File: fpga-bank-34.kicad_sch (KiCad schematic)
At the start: 5 parts

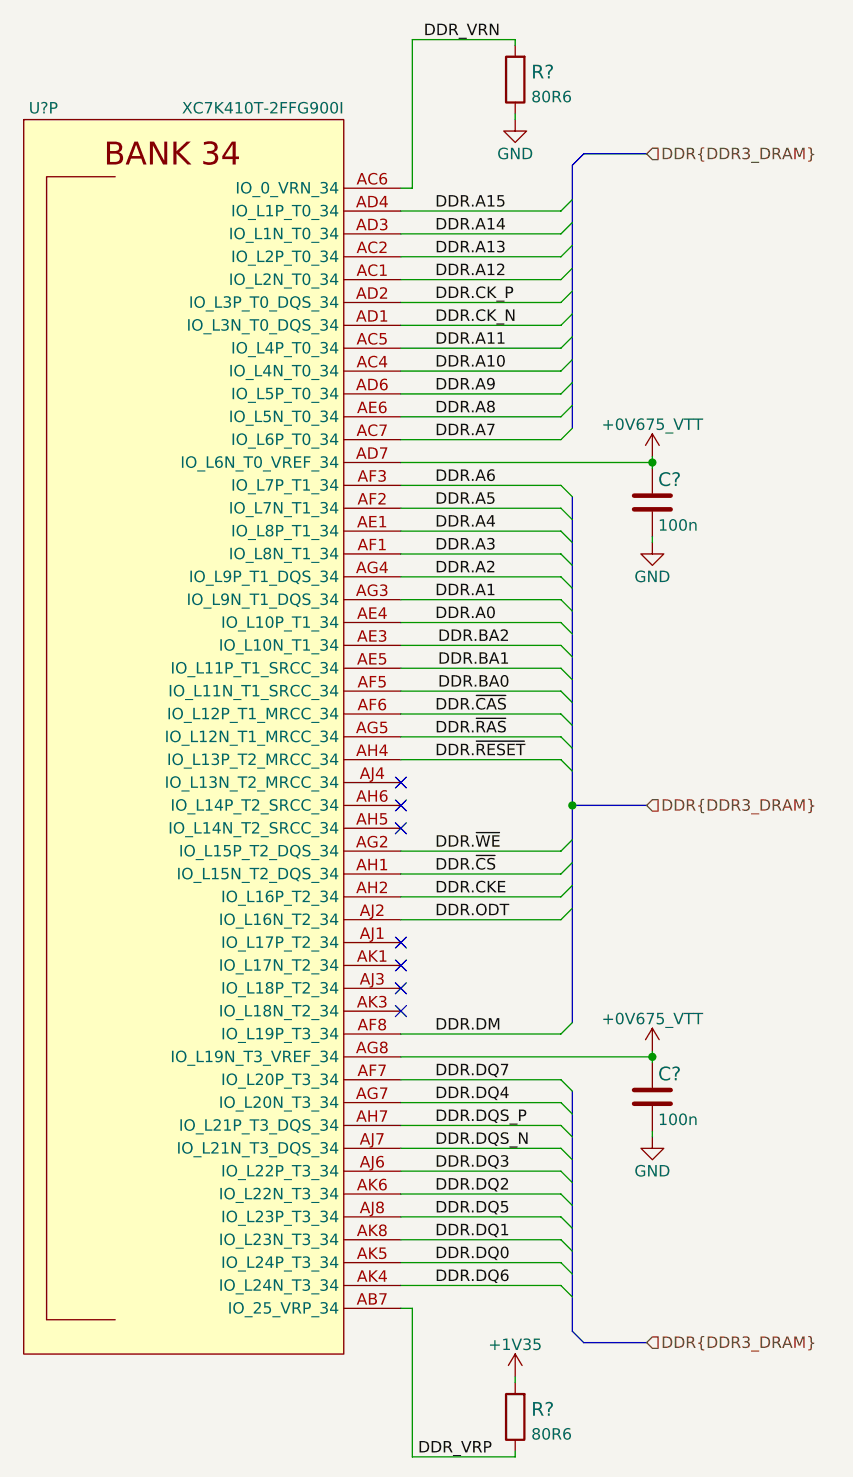
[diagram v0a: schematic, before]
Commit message: Fix FPGA symbol
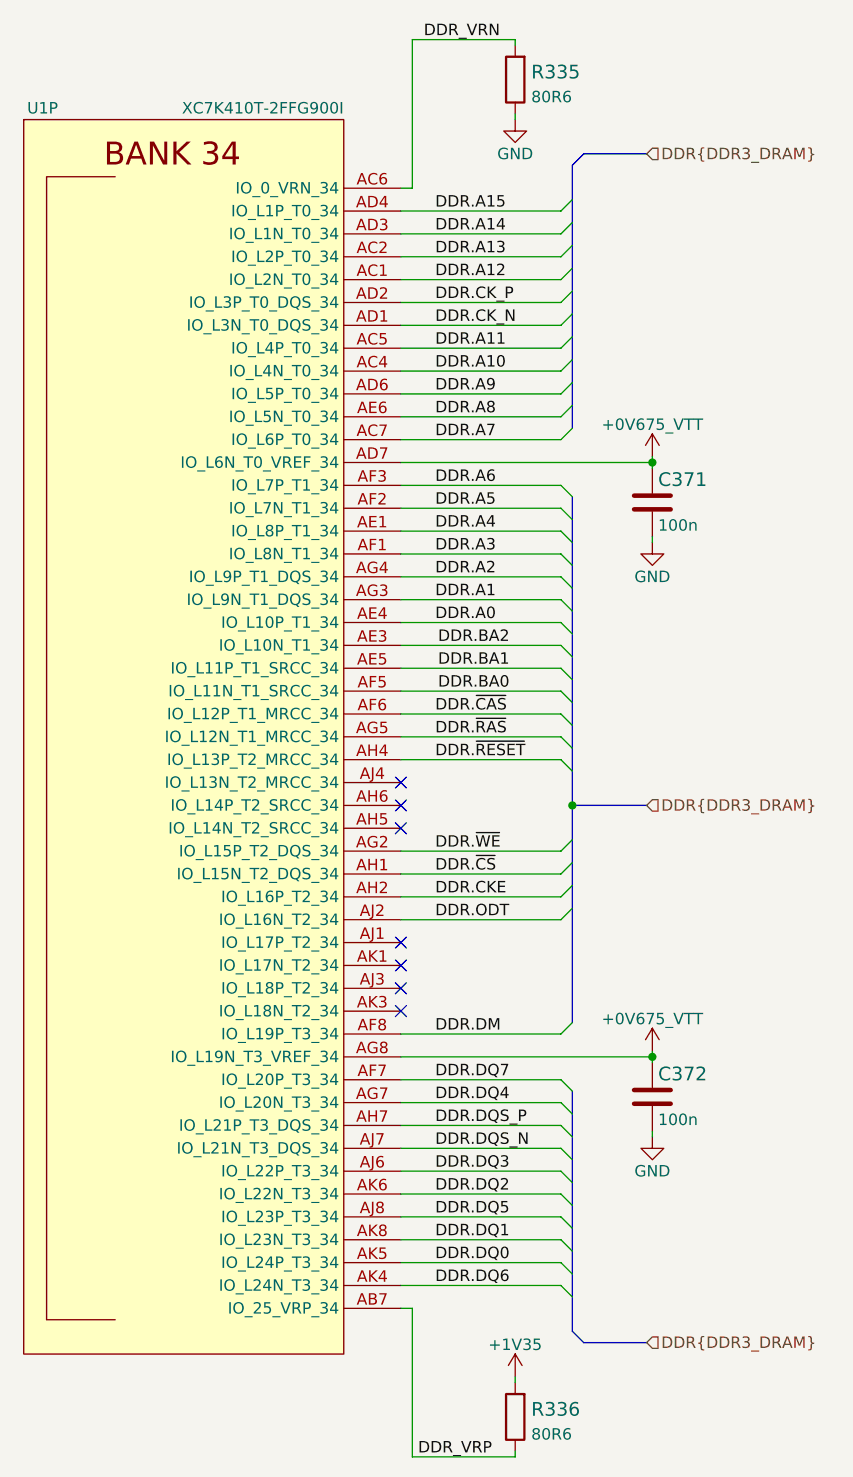
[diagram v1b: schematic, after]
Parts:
- gave numbers to parts that had none: 5
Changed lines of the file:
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@@
   (symbol (lib_id "antmicroResistors0402:R_80R6_0402") (at 156.21 71.755 90) (unit 1)
     (in_bom yes) (on_board yes) (fields_autoplaced)
-    (property "Reference" "R?" (id 0) (at 157.988 70.9204 90)
+    (property "Reference" "R335" (id 0) (at 157.988 70.9204 90)
       (effects (font (size 1.524 1.524)) (justify right))
     )
@@
   (symbol (lib_id "antmicroResistors0402:R_80R6_0402") (at 156.21 220.345 90) (unit 1)
     (in_bom yes) (on_board yes) (fields_autoplaced)
-    (property "Reference" "R?" (id 0) (at 157.988 219.5104 90)
+    (property "Reference" "R336" (id 0) (at 157.988 219.5104 90)
       (effects (font (size 1.524 1.524)) (justify right))
     )
@@
   (symbol (lib_id "power:GND") (at 171.45 189.23 0) (unit 1)
     (in_bom yes) (on_board yes)
-    (property "Reference" "#PWR?" (id 0) (at 171.45 195.58 0)
+    (property "Reference" "#PWR0513" (id 0) (at 171.45 195.58 0)
       (effects (font (size 1.27 1.27)) hide)
     )
@@
   (symbol (lib_id "power:GND") (at 171.45 123.19 0) (unit 1)
     (in_bom yes) (on_board yes)
-    (property "Reference" "#PWR?" (id 0) (at 171.45 129.54 0)
+    (property "Reference" "#PWR0512" (id 0) (at 171.45 129.54 0)
       (effects (font (size 1.27 1.27)) hide)
     )
@@
   (symbol (lib_id "antmicroPower:+0V675_VTT") (at 171.45 113.665 0) (unit 1)
     (in_bom yes) (on_board yes) (fields_autoplaced)
-    (property "Reference" "#PWR?" (id 0) (at 171.45 117.475 0)
+    (property "Reference" "#PWR0511" (id 0) (at 171.45 117.475 0)
       (effects (font (size 1.27 1.27)) hide)
     )
@@
     (pin "1")
   )
-  (symbol (lib_name "XC7K410T-2FFG900I_1") (lib_id "antmicroMicrocontrollers:XC7K410T-2FFG900I") (at 119.38 144.78 0) (unit 16)
+  (symbol (lib_id "antmicroMicrocontrollers:XC7K410T-2FFG900I") (at 119.38 144.78 0) (unit 16)
     (in_bom yes) (on_board yes)
-    (property "Reference" "U?" (id 0) (at 105.41 74.93 0)
+    (property "Reference" "U1" (id 0) (at 105.41 74.93 0)
       (effects (font (size 1.27 1.27)) (justify right))
     )
@@
   (symbol (lib_id "antmicroCapacitorsmisc:C_100n_0201") (at 171.45 184.785 0) (unit 1)
     (in_bom yes) (on_board yes)
-    (property "Reference" "C?" (id 0) (at 172.085 182.245 0)
+    (property "Reference" "C372" (id 0) (at 172.085 182.245 0)
       (effects (font (size 1.524 1.524)) (justify left))
     )
@@
   (symbol (lib_id "antmicroCapacitorsmisc:C_100n_0201") (at 171.45 118.745 0) (unit 1)
     (in_bom yes) (on_board yes)
-    (property "Reference" "C?" (id 0) (at 172.085 116.205 0)
+    (property "Reference" "C371" (id 0) (at 172.085 116.205 0)
       (effects (font (size 1.524 1.524)) (justify left))
     )
@@
   (symbol (lib_id "power:+1V35") (at 156.21 215.9 0) (unit 1)
     (in_bom yes) (on_board yes) (fields_autoplaced)
-    (property "Reference" "#PWR?" (id 0) (at 156.21 219.71 0)
+    (property "Reference" "#PWR0510" (id 0) (at 156.21 219.71 0)
       (effects (font (size 1.27 1.27)) hide)
     )
@@
   (symbol (lib_id "antmicroPower:+0V675_VTT") (at 171.45 179.705 0) (unit 1)
     (in_bom yes) (on_board yes) (fields_autoplaced)
-    (property "Reference" "#PWR?" (id 0) (at 171.45 183.515 0)
+    (property "Reference" "#PWR0514" (id 0) (at 171.45 183.515 0)
       (effects (font (size 1.27 1.27)) hide)
     )
@@
   (symbol (lib_id "power:GND") (at 156.21 76.2 0) (unit 1)
     (in_bom yes) (on_board yes)
-    (property "Reference" "#PWR?" (id 0) (at 156.21 82.55 0)
-      (effects (font (size 1.27 1.27)) hide)
-    )
+    (property "Reference" "#PWR0509" (id 0) (at 156.21 82.55 0)
+      (effects (font (size 1.27 1.27)) hide)
+    )

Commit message: Re-annotate the schematic. Export changes to PCB
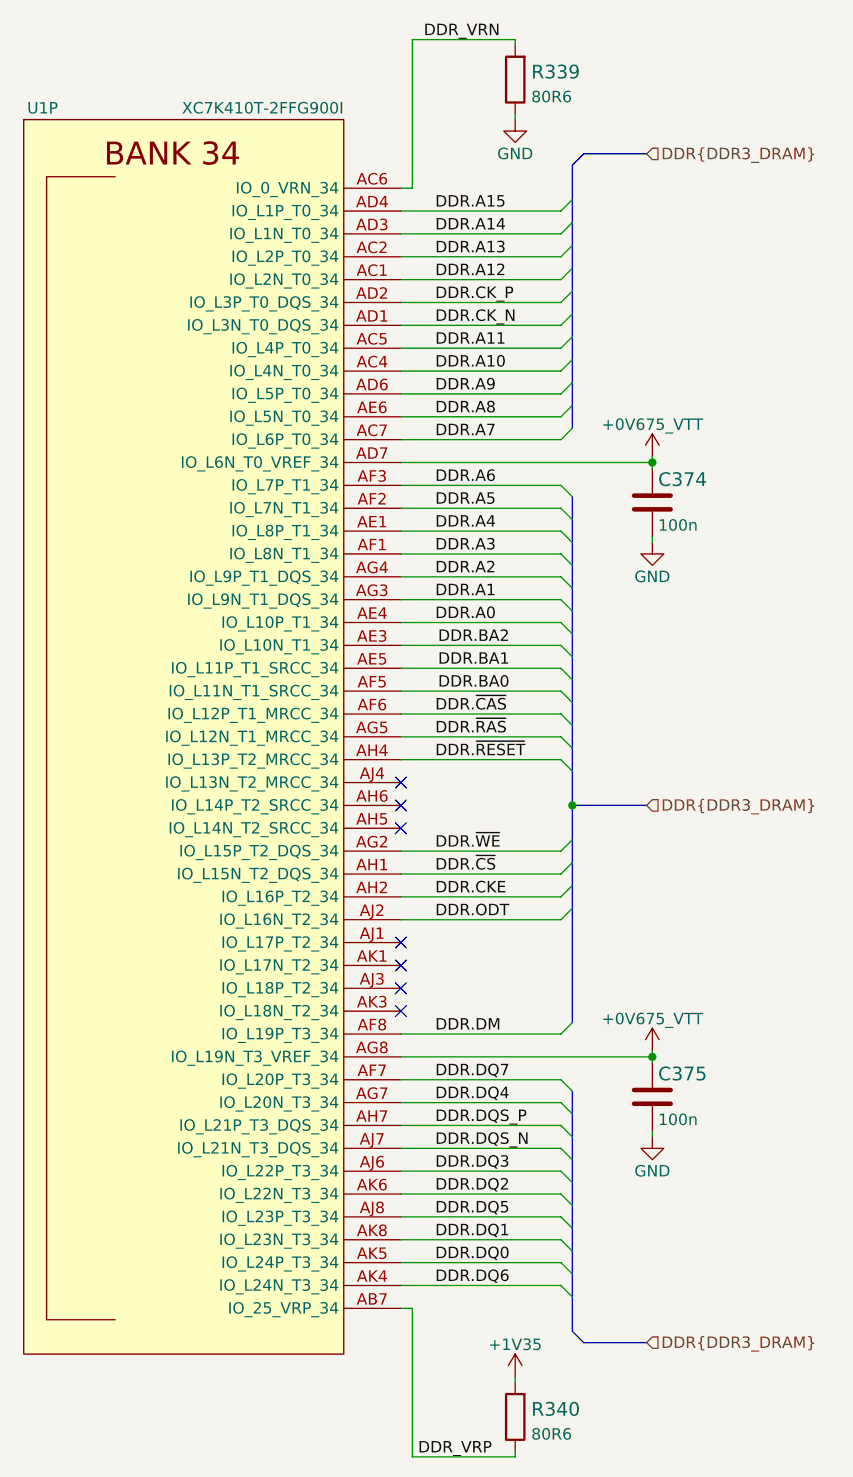
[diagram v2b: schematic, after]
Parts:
- renumbered C371 to C374, C372 to C375, R335 to R339, R336 to R340
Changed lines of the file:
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@@
   (symbol (lib_id "antmicroResistors0402:R_80R6_0402") (at 156.21 71.755 90) (unit 1)
     (in_bom yes) (on_board yes) (fields_autoplaced)
-    (property "Reference" "R335" (id 0) (at 157.988 70.9204 90)
+    (property "Reference" "R339" (id 0) (at 157.988 70.9204 90)
       (effects (font (size 1.524 1.524)) (justify right))
     )
@@
   (symbol (lib_id "antmicroResistors0402:R_80R6_0402") (at 156.21 220.345 90) (unit 1)
     (in_bom yes) (on_board yes) (fields_autoplaced)
-    (property "Reference" "R336" (id 0) (at 157.988 219.5104 90)
+    (property "Reference" "R340" (id 0) (at 157.988 219.5104 90)
       (effects (font (size 1.524 1.524)) (justify right))
     )
@@
   (symbol (lib_id "power:GND") (at 171.45 189.23 0) (unit 1)
     (in_bom yes) (on_board yes)
-    (property "Reference" "#PWR0513" (id 0) (at 171.45 195.58 0)
+    (property "Reference" "#PWR0426" (id 0) (at 171.45 195.58 0)
       (effects (font (size 1.27 1.27)) hide)
     )
@@
   (symbol (lib_id "power:GND") (at 171.45 123.19 0) (unit 1)
     (in_bom yes) (on_board yes)
-    (property "Reference" "#PWR0512" (id 0) (at 171.45 129.54 0)
+    (property "Reference" "#PWR0424" (id 0) (at 171.45 129.54 0)
       (effects (font (size 1.27 1.27)) hide)
     )
@@
   (symbol (lib_id "antmicroPower:+0V675_VTT") (at 171.45 113.665 0) (unit 1)
     (in_bom yes) (on_board yes) (fields_autoplaced)
-    (property "Reference" "#PWR0511" (id 0) (at 171.45 117.475 0)
+    (property "Reference" "#PWR0423" (id 0) (at 171.45 117.475 0)
       (effects (font (size 1.27 1.27)) hide)
     )
@@
   (symbol (lib_id "antmicroCapacitorsmisc:C_100n_0201") (at 171.45 184.785 0) (unit 1)
     (in_bom yes) (on_board yes)
-    (property "Reference" "C372" (id 0) (at 172.085 182.245 0)
+    (property "Reference" "C375" (id 0) (at 172.085 182.245 0)
       (effects (font (size 1.524 1.524)) (justify left))
     )
@@
   (symbol (lib_id "antmicroCapacitorsmisc:C_100n_0201") (at 171.45 118.745 0) (unit 1)
     (in_bom yes) (on_board yes)
-    (property "Reference" "C371" (id 0) (at 172.085 116.205 0)
+    (property "Reference" "C374" (id 0) (at 172.085 116.205 0)
       (effects (font (size 1.524 1.524)) (justify left))
     )
@@
   (symbol (lib_id "power:+1V35") (at 156.21 215.9 0) (unit 1)
     (in_bom yes) (on_board yes) (fields_autoplaced)
-    (property "Reference" "#PWR0510" (id 0) (at 156.21 219.71 0)
+    (property "Reference" "#PWR0422" (id 0) (at 156.21 219.71 0)
       (effects (font (size 1.27 1.27)) hide)
     )
@@
   (symbol (lib_id "antmicroPower:+0V675_VTT") (at 171.45 179.705 0) (unit 1)
     (in_bom yes) (on_board yes) (fields_autoplaced)
-    (property "Reference" "#PWR0514" (id 0) (at 171.45 183.515 0)
+    (property "Reference" "#PWR0425" (id 0) (at 171.45 183.515 0)
       (effects (font (size 1.27 1.27)) hide)
     )
@@
   (symbol (lib_id "power:GND") (at 156.21 76.2 0) (unit 1)
     (in_bom yes) (on_board yes)
-    (property "Reference" "#PWR0509" (id 0) (at 156.21 82.55 0)
-      (effects (font (size 1.27 1.27)) hide)
-    )
+    (property "Reference" "#PWR0421" (id 0) (at 156.21 82.55 0)
+      (effects (font (size 1.27 1.27)) hide)
+    )

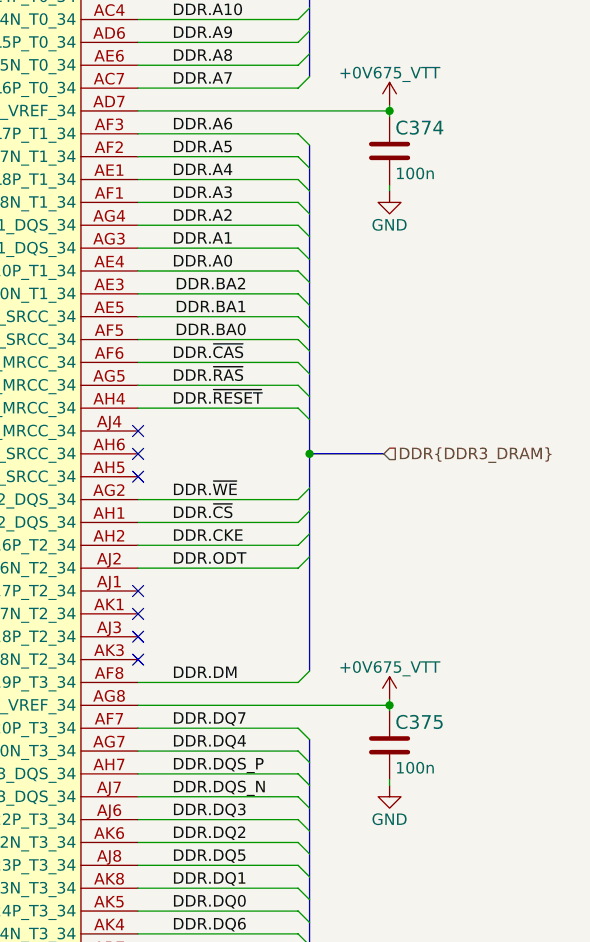
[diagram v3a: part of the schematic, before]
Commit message: Replace 100n to 0402
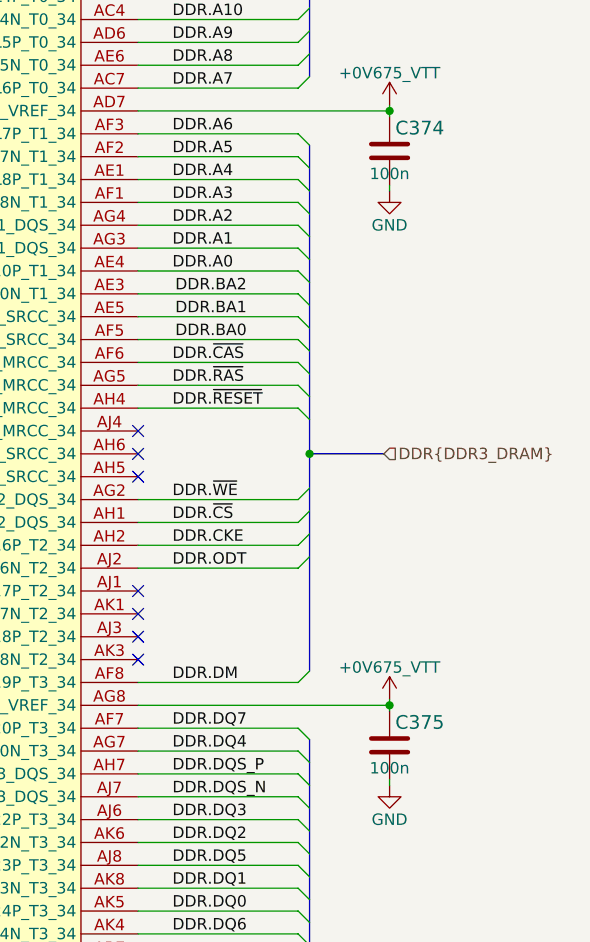
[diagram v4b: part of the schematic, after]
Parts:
- C374, C375: value C_100n_0201 -> C_100n_0402_EIA; footprint antmicro-footprints:0201-res -> antmicro-footprints:0402-cap_EIA; symbol antmicroCapacitorsmisc:C_100n_0201 -> antmicroCapacitors0402:C_100n_0402_EIA; MPN CC0201KRX6S5BB104 -> GRM155R61H104KE14D; Manufacturer YAGEO -> Murata
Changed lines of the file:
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@@
     (pin "AK8")
   )
-  (symbol (lib_id "antmicroCapacitorsmisc:C_100n_0201") (at 171.45 184.785 0) (unit 1)
+  (symbol (lib_id "antmicroCapacitors0402:C_100n_0402_EIA") (at 171.45 184.785 0) (unit 1)
     (in_bom yes) (on_board yes)
     (property "Reference" "C375" (id 0) (at 172.085 182.245 0)
       (effects (font (size 1.524 1.524)) (justify left))
     )
-    (property "Value" "C_100n_0201" (id 1) (at 171.45 188.595 0)
+    (property "Value" "C_100n_0402_EIA" (id 1) (at 171.45 188.595 0)
       (effects (font (size 1.524 1.524)) hide)
     )
-    (property "Footprint" "antmicro-footprints:0201-res" (id 2) (at 176.53 179.705 0)
+    (property "Footprint" "antmicro-footprints:0402-cap_EIA" (id 2) (at 176.53 179.705 0)
       (effects (font (size 1.524 1.524)) (justify left) hide)
     )
@@
       (effects (font (size 1.27 1.27)) hide)
     )
-    (property "Manufacturer" "YAGEO" (id 4) (at 176.53 174.625 0)
+    (property "Manufacturer" "Murata" (id 4) (at 176.53 174.625 0)
       (effects (font (size 1.524 1.524)) (justify left) hide)
     )
-    (property "MPN" "CC0201KRX6S5BB104" (id 5) (at 176.53 177.165 0)
+    (property "MPN" "GRM155R61H104KE14D" (id 5) (at 176.53 177.165 0)
       (effects (font (size 1.524 1.524)) (justify left) hide)
     )
-    (property "Val" "100n" (id 6) (at 172.085 187.325 0)
-      (effects (font (size 1.27 1.27)) (justify left))
-    )
+    (property "Val" "100n" (id 6) (at 171.45 187.325 0))
     (pin "1")
     (pin "2")
   )
-  (symbol (lib_id "antmicroCapacitorsmisc:C_100n_0201") (at 171.45 118.745 0) (unit 1)
+  (symbol (lib_id "antmicroCapacitors0402:C_100n_0402_EIA") (at 171.45 118.745 0) (unit 1)
     (in_bom yes) (on_board yes)
     (property "Reference" "C374" (id 0) (at 172.085 116.205 0)
       (effects (font (size 1.524 1.524)) (justify left))
     )
-    (property "Value" "C_100n_0201" (id 1) (at 171.45 122.555 0)
+    (property "Value" "C_100n_0402_EIA" (id 1) (at 171.45 122.555 0)
       (effects (font (size 1.524 1.524)) hide)
     )
-    (property "Footprint" "antmicro-footprints:0201-res" (id 2) (at 176.53 113.665 0)
+    (property "Footprint" "antmicro-footprints:0402-cap_EIA" (id 2) (at 176.53 113.665 0)
       (effects (font (size 1.524 1.524)) (justify left) hide)
     )
@@
       (effects (font (size 1.27 1.27)) hide)
     )
-    (property "Manufacturer" "YAGEO" (id 4) (at 176.53 108.585 0)
+    (property "Manufacturer" "Murata" (id 4) (at 176.53 108.585 0)
       (effects (font (size 1.524 1.524)) (justify left) hide)
     )
-    (property "MPN" "CC0201KRX6S5BB104" (id 5) (at 176.53 111.125 0)
+    (property "MPN" "GRM155R61H104KE14D" (id 5) (at 176.53 111.125 0)
       (effects (font (size 1.524 1.524)) (justify left) hide)
     )
-    (property "Val" "100n" (id 6) (at 172.085 121.285 0)
-      (effects (font (size 1.27 1.27)) (justify left))
-    )
+    (property "Val" "100n" (id 6) (at 171.45 121.285 0))
     (pin "1")
     (pin "2")
